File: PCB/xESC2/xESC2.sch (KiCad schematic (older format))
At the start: 0 parts

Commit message: wip
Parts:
- added H1, H2, H3, H4: MountingHole_Pad, MountingHole:MountingHole_2.7mm_M2.5_DIN965_Pad, symbol Mechanical:MountingHole_Pad
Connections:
- new net GND: H1.1, H2.1, H3.1, H4.1
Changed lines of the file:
@@
 $EndDescr
 $Sheet
-S 6000 1950 1650 2050
+S 8800 1400 1550 2550
 U 61A3F4E8
 F0 "Power" 50
 F1 "Power.sch" 50
+F2 "DRV_ENABLE" I L 8800 2050 50
+F3 "NCS" I L 8800 2150 50
+F4 "SCK" I L 8800 2250 50
+F5 "MOSI" I L 8800 2350 50
+F6 "MISO" O L 8800 2450 50
+F7 "UH" I L 8800 2700 50
+F8 "UL" I L 8800 2800 50
+F9 "VH" I L 8800 2900 50
+F10 "VL" I L 8800 3000 50
+F11 "WH" I L 8800 3100 50
+F12 "WL" I L 8800 3200 50
+F13 "FAULT" O L 8800 3400 50
+F14 "CURU_5V" O L 8800 3550 50
+F15 "CURV_5V" O L 8800 3650 50
+F16 "CURW_5V" O L 8800 3750 50
+F17 "VCCIO" I L 8800 1850 50
+F18 "5V_OUT" O L 8800 1650 50
+F19 "3V3_OUT" O L 8800 1750 50
+F20 "VM" O L 8800 1550 50
 $EndSheet
+Wire Wire Line
+	8800 1750 8550 1750
+Wire Wire Line
+	8550 1750 8550 1850
+Wire Wire Line
+	8550 1850 8800 1850
+$Comp
+L Mechanical:MountingHole_Pad H1
+U 1 1 61DB61D0
+P 8600 5750
+F 0 "H1" H 8700 5799 50  0000 L CNN
+F 1 "MountingHole_Pad" H 8700 5708 50  0000 L CNN
+F 2 "MountingHole:MountingHole_2.7mm_M2.5_DIN965_Pad" H 8600 5750 50  0001 C CNN
+F 3 "~" H 8600 5750 50  0001 C CNN
+	1    8600 5750
+	1    0    0    -1
+$EndComp
+$Comp
+L Mechanical:MountingHole_Pad H2
+U 1 1 61DB6764
+P 8850 5750
+F 0 "H2" H 8950 5799 50  0000 L CNN
+F 1 "MountingHole_Pad" H 8950 5708 50  0000 L CNN
+F 2 "MountingHole:MountingHole_2.7mm_M2.5_DIN965_Pad" H 8850 5750 50  0001 C CNN
+F 3 "~" H 8850 5750 50  0001 C CNN
+	1    8850 5750
+	1    0    0    -1
+$EndComp
+$Comp
+L Mechanical:MountingHole_Pad H3
+U 1 1 61DB6A4D
+P 9100 5750
+F 0 "H3" H 9200 5799 50  0000 L CNN
+F 1 "MountingHole_Pad" H 9200 5708 50  0000 L CNN
+F 2 "MountingHole:MountingHole_2.7mm_M2.5_DIN965_Pad" H 9100 5750 50  0001 C CNN
+F 3 "~" H 9100 5750 50  0001 C CNN
+	1    9100 5750
+	1    0    0    -1
+$EndComp
+$Comp
+L Mechanical:MountingHole_Pad H4
+U 1 1 61DB6BE9
+P 9350 5750
+F 0 "H4" H 9450 5799 50  0000 L CNN
+F 1 "MountingHole_Pad" H 9450 5708 50  0000 L CNN
+F 2 "MountingHole:MountingHole_2.7mm_M2.5_DIN965_Pad" H 9350 5750 50  0001 C CNN
+F 3 "~" H 9350 5750 50  0001 C CNN
+	1    9350 5750
+	1    0    0    -1
+$EndComp
+Wire Wire Line
+	8600 5850 8600 6150
+Wire Wire Line
+	8600 6150 8850 6150
+Wire Wire Line
+	9350 6150 9350 5850
+Wire Wire Line
+	9100 5850 9100 6150
+Connection ~ 9100 6150
+Wire Wire Line
+	9100 6150 9350 6150
+Wire Wire Line
+	8850 6150 8850 5850
+Connection ~ 8850 6150
+Wire Wire Line
+	8850 6150 9100 6150
+$Comp
+L power:GND #PWR0119
+U 1 1 61DB7185
+P 8850 6300
+F 0 "#PWR0119" H 8850 6050 50  0001 C CNN
+F 1 "GND" H 8855 6127 50  0000 C CNN
+F 2 "" H 8850 6300 50  0001 C CNN
+F 3 "" H 8850 6300 50  0001 C CNN
+	1    8850 6300
+	1    0    0    -1
+$EndComp
+Wire Wire Line
+	8850 6300 8850 6150
 $EndSCHEMATC

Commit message: wip power xESC2
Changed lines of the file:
@@
 $Descr A4 11693 8268
 encoding utf-8
-Sheet 1 5
+Sheet 1 7
 Title ""
 Date ""
@@
 F16 "CURW_5V" O L 8800 3750 50
 F17 "VCCIO" I L 8800 1850 50
-F18 "5V_OUT" O L 8800 1650 50
-F19 "3V3_OUT" O L 8800 1750 50
-F20 "VM" O L 8800 1550 50
+F18 "VM" O L 8800 1550 50
 $EndSheet
-Wire Wire Line
-	8800 1750 8550 1750
-Wire Wire Line
-	8550 1750 8550 1850
-Wire Wire Line
-	8550 1850 8800 1850
 $Comp
 L Mechanical:MountingHole_Pad H1
@@
 Wire Wire Line
 	8850 6300 8850 6150
+$Sheet
+S 4300 4200 1000 1150
+U 61E7227A
+F0 "VREG" 50
+F1 "VREG.sch" 50
+F2 "5V_OUT" O L 4300 4400 50
+F3 "3V3_OUT" O L 4300 4500 50
+F4 "VIN" I L 4300 4300 50
+$EndSheet
+$Sheet
+S 3250 1450 1400 2050
+U 61AC26FB
+F0 "MCU" 50
+F1 "MCU.sch" 50
+$EndSheet
 $EndSCHEMATC

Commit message: wip xESC2 logic
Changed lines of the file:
@@
 	8850 6300 8850 6150
 $Sheet
-S 4300 4200 1000 1150
+S 8800 4150 1000 1150
 U 61E7227A
 F0 "VREG" 50
 F1 "VREG.sch" 50
-F2 "5V_OUT" O L 4300 4400 50
-F3 "3V3_OUT" O L 4300 4500 50
-F4 "VIN" I L 4300 4300 50
+F2 "5V_OUT" O L 8800 4350 50
+F3 "3V3_OUT" O L 8800 4450 50
+F4 "VIN" I L 8800 4250 50
 $EndSheet
 $Sheet
@@
 F1 "MCU.sch" 50
 $EndSheet
+Wire Wire Line
+	8800 4250 8550 4250
+Wire Wire Line
+	8550 4250 8550 1550
+Wire Wire Line
+	8550 1550 8800 1550
+Wire Wire Line
+	8800 1850 8500 1850
+Wire Wire Line
+	8500 1850 8500 4450
+Wire Wire Line
+	8500 4450 8800 4450
+$Comp
+L power:+3.3V #PWR0121
+U 1 1 61A9C40A
+P 8200 4050
+F 0 "#PWR0121" H 8200 3900 50  0001 C CNN
+F 1 "+3.3V" H 8215 4223 50  0000 C CNN
+F 2 "" H 8200 4050 50  0001 C CNN
+F 3 "" H 8200 4050 50  0001 C CNN
+	1    8200 4050
+	1    0    0    -1
+$EndComp
+$Comp
+L power:+5V #PWR0122
+U 1 1 61A9D303
+P 8400 4050
+F 0 "#PWR0122" H 8400 3900 50  0001 C CNN
+F 1 "+5V" H 8415 4223 50  0000 C CNN
+F 2 "" H 8400 4050 50  0001 C CNN
+F 3 "" H 8400 4050 50  0001 C CNN
+	1    8400 4050
+	1    0    0    -1
+$EndComp
+Wire Wire Line
+	8400 4050 8400 4350
+Wire Wire Line
+	8400 4350 8800 4350
+Wire Wire Line
+	8200 4050 8200 4450
+Wire Wire Line
+	8200 4450 8500 4450
+Connection ~ 8500 4450
 $EndSCHEMATC

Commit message: wip logic
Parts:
- added C15, C27, C28, C29, C30, C31: DNP, Capacitor_SMD:C_0603_1608Metric, symbol Device:C
- added R17, R18, R19, R20, R21, R22, R23, R24, R25, R26, R27, R28: R, Resistor_SMD:R_0603_1608Metric, symbol Device:R
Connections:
- net GND: now also C15.2, C27.2, C28.2, C29.2, C30.2, C31.2, R18.2, R20.2, R22.2, R24.2, R26.2, R28.2
- new net CURU_5V: R17.1
- new net CURV_5V: R19.1
- new net CURW_5V: R21.1
- new net CUR_U: C15.1, R17.2, R18.1
- new net CUR_V: C27.1, R19.2, R20.1
- new net CUR_W: C28.1, R21.2, R22.1
- new net PHASE_U_FILTERED: C29.1, R23.2, R24.1
- new net PHASE_U_RAW: R23.1
- new net PHASE_V_FILTERED: C30.1, R25.2, R26.1
- new net PHASE_V_RAW: R25.1
- new net PHASE_W_FILTERED: C31.1, R27.2, R28.1
- new net PHASE_W_RAW: R27.1
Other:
- moved on the sheet: H1, H2, H3, H4

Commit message: wip
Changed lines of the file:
@@
 $EndSheet
 $Sheet
-S 4550 1400 1650 3250
+S 4550 1400 1650 3800
 U 61AC26FB
 F0 "MCU" 50
@@
 F29 "DRV_NCS" O R 6200 2150 50
 F30 "DRV_SCK" O R 6200 2250 50
+F31 "AN_IN" I L 4550 3900 50
+F32 "TEMP_MOTOR" I L 4550 4100 50
+F33 "HALL_3" I L 4550 4400 50
+F34 "HALL_2" I L 4550 4300 50
+F35 "HALL_1" I L 4550 4200 50
+F36 "SCK_EXT" O L 4550 4850 50
+F37 "MISO_EXT" I L 4550 4650 50
+F38 "TX_MOSI_EXT" O L 4550 4750 50
+F39 "RX_NCS_EXT" I L 4550 4950 50
 $EndSheet
 Wire Wire Line

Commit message: wip V2.0
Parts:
- added C44: 100nF/50V, Capacitor_SMD:C_0603_1608Metric, symbol Device:C
- added C45, C46, C47: DNP, Capacitor_SMD:C_0603_1608Metric, symbol Device:C
- added D3: D_Schottky, Diode_SMD:D_SOD-123, symbol Device:D_Schottky
- added D4, D5: LED, LED_SMD:LED_0603_1608Metric, symbol Device:LED
- added J1: Conn_01x06_Male, Connector_PinHeader_2.54mm:PinHeader_1x06_P2.54mm_Vertical, symbol Connector:Conn_01x06_Male
- added J2: U254-051T-4BH83-F1S, USB:XKB_U254-051T-4BH83-F1S, symbol U254-051T-4BH83-F1S:U254-051T-4BH83-F1S
- added J3, J4: Conn_01x05_Male, Connector_PinHeader_2.54mm:PinHeader_1x05_P2.54mm_Vertical, symbol Connector:Conn_01x05_Male
- added J5: Conn_01x03_Male, Connector_PinHeader_2.54mm:PinHeader_1x03_P2.54mm_Vertical, symbol Connector:Conn_01x03_Male
- added R30, R33, R34, R35, R36: R, Resistor_SMD:R_0603_1608Metric, symbol Device:R
- added R31, R32: 22R, Resistor_SMD:R_0603_1608Metric, symbol Device:R
- added R37, R38: 150R, Resistor_SMD:R_0603_1608Metric, symbol Device:R
- added U5: SN65HVD232, Package_SO:SOIC-8_3.9x4.9mm_P1.27mm, symbol Interface_CAN_LIN:SN65HVD232
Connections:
- net +3V3: now also J3.1 (Pin_1), R30.1, U5.3 (VCC)
- net +5V: now also D3.1 (K), J1.1 (Pin_1), R33.1, R34.1, R35.1
- net GND: now also C44.2, C45.2, C46.2, C47.2, D4.1 (K), D5.1 (K), J1.6 (Pin_6), J2.5 (GND), J2.S1 (SHIELD), J2.S2 (SHIELD), J2.S3 (SHIELD), J2.S4 (SHIELD), J2.S5 (SHIELD), J2.S6 (SHIELD), J3.3 (Pin_3), J4.5 (Pin_5), J5.1 (Pin_1), U5.2 (GND)
- net MCU/CAN_RX: now also U5.4 (R)
- net MCU/CAN_TX: now also U5.1 (D)
- net MCU/MISO_EXT: now also J4.1 (Pin_1)
- net MCU/RX_NCS_EXT: now also J4.4 (Pin_4)
- net MCU/Reset: now also J3.5 (Pin_5)
- net MCU/SCK_EXT: now also J4.3 (Pin_3)
- net MCU/SWDCLK: now also J3.2 (Pin_2)
- net MCU/SWDIO: now also J3.4 (Pin_4)
- net MCU/TX_MOSI_EXT: now also J4.2 (Pin_2)
- new net: D3.2 (A), J2.1 (VCC)
- new net: J2.2 (D-), R31.2
- new net: J2.3 (D+), R32.2
- new net: J5.2 (Pin_2), R36.2, U5.6 (CANL)
- new net: J5.3 (Pin_3), R36.1, U5.7 (CANH)
- new net: D4.2 (A), R37.2
- new net: D5.2 (A), R38.2
- new net HALL1: C45.1, J1.3 (Pin_3), R33.2
- new net HALL2: C46.1, J1.4 (Pin_4), R34.2
- new net HALL3: C47.1, J1.5 (Pin_5), R35.2
- new net LED_GREEN: R37.1
- new net LED_RED: R38.1
- new net TEMP_MOTOR: C44.1, J1.2 (Pin_2), R30.2
- new net USB_DM: R31.1
- new net USB_DP: R32.1
- no-connect marks 0 -> 1

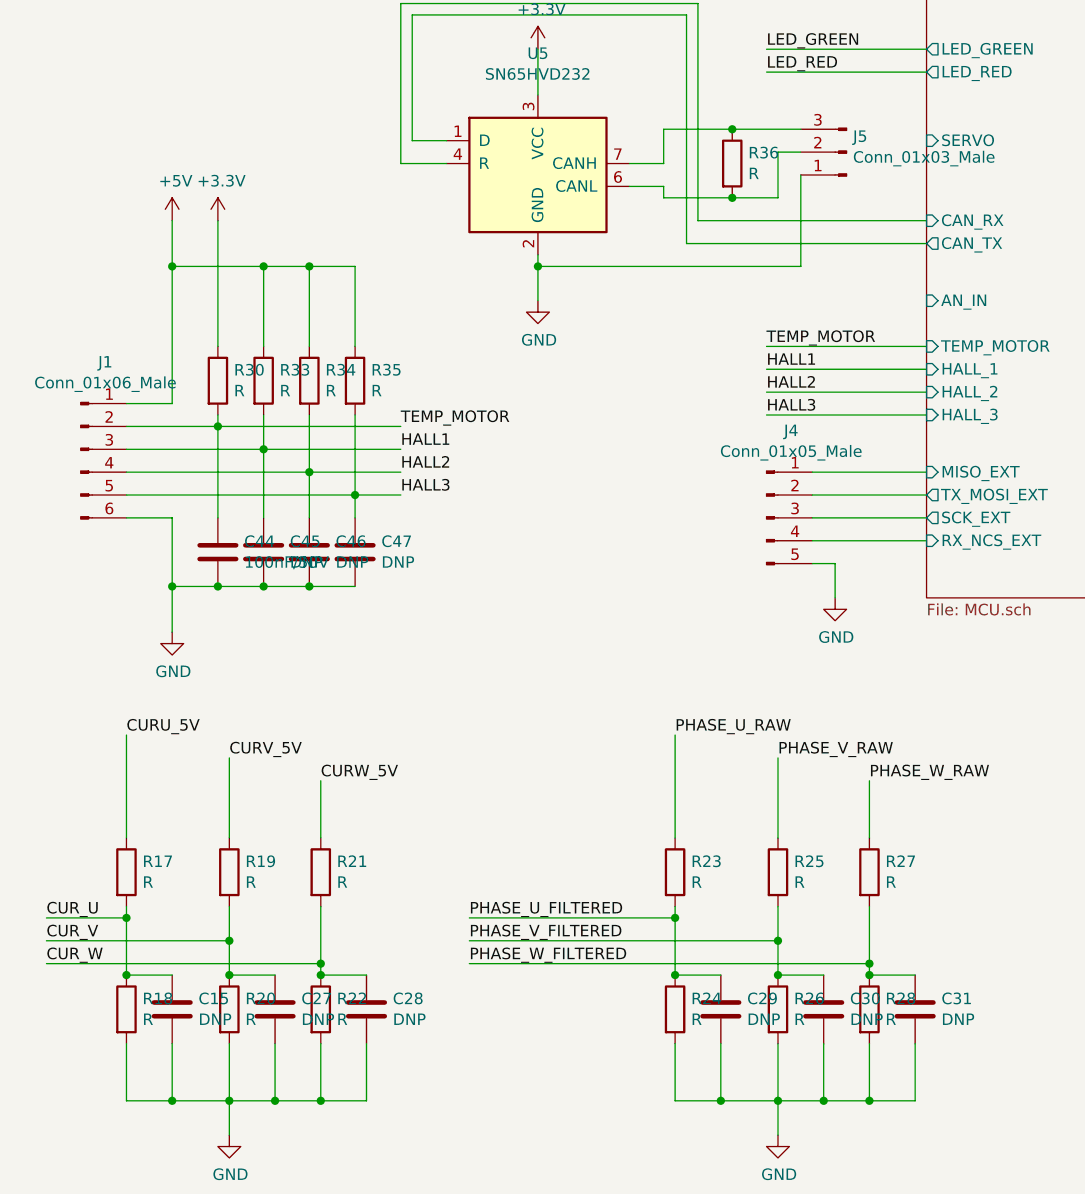
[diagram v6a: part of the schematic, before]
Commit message: changed some values, added BOM
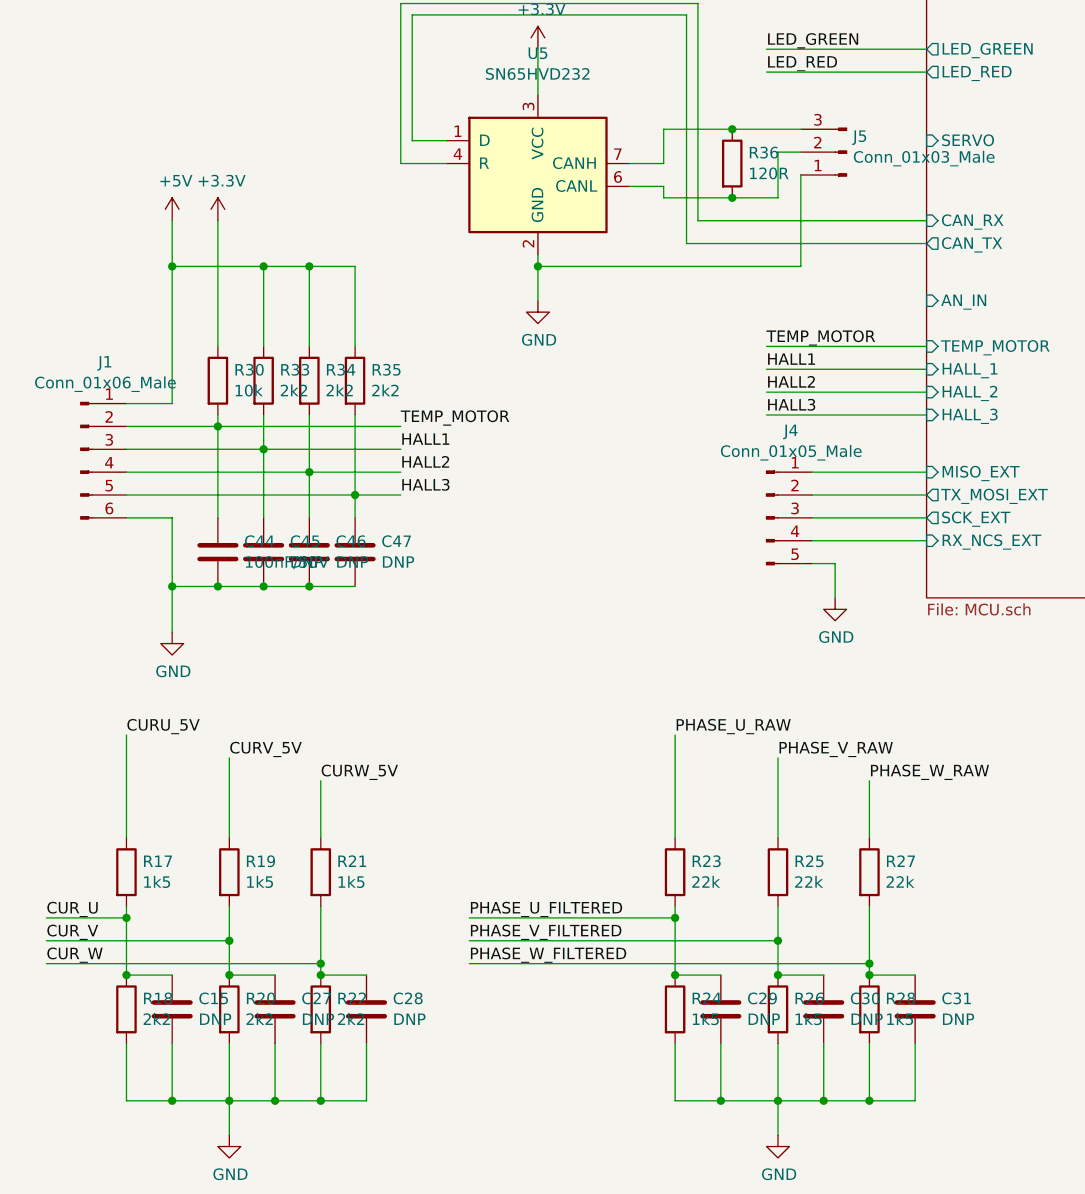
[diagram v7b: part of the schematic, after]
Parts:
- R17, R19, R21, R24, R26, R28: value R -> 1k5
- R18, R20, R22, R33, R34, R35: value R -> 2k2
- R23, R25, R27: value R -> 22k
- R30: value R -> 10k
- R36: value R -> 120R
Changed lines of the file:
@@
 P 1050 6400
 F 0 "R17" H 1120 6446 50  0000 L CNN
-F 1 "R" H 1120 6355 50  0000 L CNN
+F 1 "1k5" H 1120 6355 50  0000 L CNN
 F 2 "Resistor_SMD:R_0603_1608Metric" V 980 6400 50  0001 C CNN
 F 3 "~" H 1050 6400 50  0001 C CNN
@@
 P 1050 7000
 F 0 "R18" H 1120 7046 50  0000 L CNN
-F 1 "R" H 1120 6955 50  0000 L CNN
+F 1 "2k2" H 1120 6955 50  0000 L CNN
 F 2 "Resistor_SMD:R_0603_1608Metric" V 980 7000 50  0001 C CNN
 F 3 "~" H 1050 7000 50  0001 C CNN
@@
 P 1500 6400
 F 0 "R19" H 1570 6446 50  0000 L CNN
-F 1 "R" H 1570 6355 50  0000 L CNN
+F 1 "1k5" H 1570 6355 50  0000 L CNN
 F 2 "Resistor_SMD:R_0603_1608Metric" V 1430 6400 50  0001 C CNN
 F 3 "~" H 1500 6400 50  0001 C CNN
@@
 P 1500 7000
 F 0 "R20" H 1570 7046 50  0000 L CNN
-F 1 "R" H 1570 6955 50  0000 L CNN
+F 1 "2k2" H 1570 6955 50  0000 L CNN
 F 2 "Resistor_SMD:R_0603_1608Metric" V 1430 7000 50  0001 C CNN
 F 3 "~" H 1500 7000 50  0001 C CNN
@@
 P 1900 6400
 F 0 "R21" H 1970 6446 50  0000 L CNN
-F 1 "R" H 1970 6355 50  0000 L CNN
+F 1 "1k5" H 1970 6355 50  0000 L CNN
 F 2 "Resistor_SMD:R_0603_1608Metric" V 1830 6400 50  0001 C CNN
 F 3 "~" H 1900 6400 50  0001 C CNN
@@
 P 1900 7000
 F 0 "R22" H 1970 7046 50  0000 L CNN
-F 1 "R" H 1970 6955 50  0000 L CNN
+F 1 "2k2" H 1970 6955 50  0000 L CNN
 F 2 "Resistor_SMD:R_0603_1608Metric" V 1830 7000 50  0001 C CNN
 F 3 "~" H 1900 7000 50  0001 C CNN
@@
 P 3450 6400
 F 0 "R23" H 3520 6446 50  0000 L CNN
-F 1 "R" H 3520 6355 50  0000 L CNN
+F 1 "22k" H 3520 6355 50  0000 L CNN
 F 2 "Resistor_SMD:R_0603_1608Metric" V 3380 6400 50  0001 C CNN
 F 3 "~" H 3450 6400 50  0001 C CNN
@@
 P 3450 7000
 F 0 "R24" H 3520 7046 50  0000 L CNN
-F 1 "R" H 3520 6955 50  0000 L CNN
+F 1 "1k5" H 3520 6955 50  0000 L CNN
 F 2 "Resistor_SMD:R_0603_1608Metric" V 3380 7000 50  0001 C CNN
 F 3 "~" H 3450 7000 50  0001 C CNN
@@
 P 3900 6400
 F 0 "R25" H 3970 6446 50  0000 L CNN
-F 1 "R" H 3970 6355 50  0000 L CNN
+F 1 "22k" H 3970 6355 50  0000 L CNN
 F 2 "Resistor_SMD:R_0603_1608Metric" V 3830 6400 50  0001 C CNN
 F 3 "~" H 3900 6400 50  0001 C CNN
@@
 P 3900 7000
 F 0 "R26" H 3970 7046 50  0000 L CNN
-F 1 "R" H 3970 6955 50  0000 L CNN
+F 1 "1k5" H 3970 6955 50  0000 L CNN
 F 2 "Resistor_SMD:R_0603_1608Metric" V 3830 7000 50  0001 C CNN
 F 3 "~" H 3900 7000 50  0001 C CNN
@@
 P 4300 6400
 F 0 "R27" H 4370 6446 50  0000 L CNN
-F 1 "R" H 4370 6355 50  0000 L CNN
+F 1 "22k" H 4370 6355 50  0000 L CNN
 F 2 "Resistor_SMD:R_0603_1608Metric" V 4230 6400 50  0001 C CNN
 F 3 "~" H 4300 6400 50  0001 C CNN
@@
 P 4300 7000
 F 0 "R28" H 4370 7046 50  0000 L CNN
-F 1 "R" H 4370 6955 50  0000 L CNN
+F 1 "1k5" H 4370 6955 50  0000 L CNN
 F 2 "Resistor_SMD:R_0603_1608Metric" V 4230 7000 50  0001 C CNN
 F 3 "~" H 4300 7000 50  0001 C CNN
@@
 P 1450 4250
 F 0 "R30" H 1520 4296 50  0000 L CNN
-F 1 "R" H 1520 4205 50  0000 L CNN
+F 1 "10k" H 1520 4205 50  0000 L CNN
 F 2 "Resistor_SMD:R_0603_1608Metric" V 1380 4250 50  0001 C CNN
 F 3 "~" H 1450 4250 50  0001 C CNN
@@
 P 1650 4250
 F 0 "R33" H 1720 4296 50  0000 L CNN
-F 1 "R" H 1720 4205 50  0000 L CNN
+F 1 "2k2" H 1720 4205 50  0000 L CNN
 F 2 "Resistor_SMD:R_0603_1608Metric" V 1580 4250 50  0001 C CNN
 F 3 "~" H 1650 4250 50  0001 C CNN
@@
 P 1850 4250
 F 0 "R34" H 1920 4296 50  0000 L CNN
-F 1 "R" H 1920 4205 50  0000 L CNN
+F 1 "2k2" H 1920 4205 50  0000 L CNN
 F 2 "Resistor_SMD:R_0603_1608Metric" V 1780 4250 50  0001 C CNN
 F 3 "~" H 1850 4250 50  0001 C CNN
@@
 P 2050 4250
 F 0 "R35" H 2120 4296 50  0000 L CNN
-F 1 "R" H 2120 4205 50  0000 L CNN
+F 1 "2k2" H 2120 4205 50  0000 L CNN
 F 2 "Resistor_SMD:R_0603_1608Metric" V 1980 4250 50  0001 C CNN
 F 3 "~" H 2050 4250 50  0001 C CNN
@@
 P 3700 3300
 F 0 "R36" H 3770 3346 50  0000 L CNN
-F 1 "R" H 3770 3255 50  0000 L CNN
+F 1 "120R" H 3770 3255 50  0000 L CNN
 F 2 "Resistor_SMD:R_0603_1608Metric" V 3630 3300 50  0001 C CNN
 F 3 "~" H 3700 3300 50  0001 C CNN

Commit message: added missing resistors
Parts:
- added R39: 22k, Resistor_SMD:R_0603_1608Metric, symbol Device:R
- added R40: 1k5, Resistor_SMD:R_0603_1608Metric, symbol Device:R
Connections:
- net GND: now also R40.2
- new net VM: R39.1
- new net V_M_FILTERED: R39.2, R40.1
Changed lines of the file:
@@
 Wire Wire Line
 	7150 6300 7300 6300
+$Comp
+L Device:R R39
+U 1 1 61BE05DB
+P 5100 6400
+F 0 "R39" H 5170 6446 50  0000 L CNN
+F 1 "22k" H 5170 6355 50  0000 L CNN
+F 2 "Resistor_SMD:R_0603_1608Metric" V 5030 6400 50  0001 C CNN
+F 3 "~" H 5100 6400 50  0001 C CNN
+	1    5100 6400
+	1    0    0    -1
+$EndComp
+$Comp
+L Device:R R40
+U 1 1 61BEBE83
+P 5100 7000
+F 0 "R40" H 5170 7046 50  0000 L CNN
+F 1 "1k5" H 5170 6955 50  0000 L CNN
+F 2 "Resistor_SMD:R_0603_1608Metric" V 5030 7000 50  0001 C CNN
+F 3 "~" H 5100 7000 50  0001 C CNN
+	1    5100 7000
+	1    0    0    -1
+$EndComp
+Wire Wire Line
+	5100 7400 5100 7150
+Wire Wire Line
+	5100 7400 4500 7400
+Connection ~ 4500 7400
+Wire Wire Line
+	5100 6850 5100 6650
+Wire Wire Line
+	5100 6250 5100 6100
+Wire Wire Line
+	8550 1550 8550 1200
+Connection ~ 8550 1550
+Text Label 8550 1200 0    50   ~ 0
+VM
+Text Label 5100 6100 0    50   ~ 0
+VM
+Wire Wire Line
+	4550 3900 3850 3900
+Wire Wire Line
+	5100 6650 5750 6650
+Connection ~ 5100 6650
+Wire Wire Line
+	5100 6650 5100 6550
+Text Label 5750 6650 0    50   ~ 0
+V_M_FILTERED
+Text Label 3850 3900 0    50   ~ 0
+V_M_FILTERED
 $EndSCHEMATC
